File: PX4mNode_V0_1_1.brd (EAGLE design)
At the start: 48.6 x 34.9 mm, 135 parts, among them J201 DF13C-6P-1.25V, J202 DF13C-6P-1.25V, J203 DF13C-6P-1.25V, J301 DF13C-4P-1.25V, J401 DF13C-7P-1.25V, J402 DF13-4P-1.25V, J403 DF13C-4P-1.25V, J404 DF13C-4P-1.25V, J405 DF13C-4P-1.25V, J801 DF13C-3P-1.25V, M3_MOUNT1101 MOUNT-HOLE3.1MM, M3_MOUNT1102 MOUNT-HOLE3.1MM, M3_MOUNT1103 MOUNT-HOLE3.1MM, M3_MOUNT1104 MOUNT-HOLE3.1MM, U101 STM32F4X7VX, U401 MAX3051, U402 MAX3051, X101 3.2x2.5 mm / 24 MHz / 15 ppm

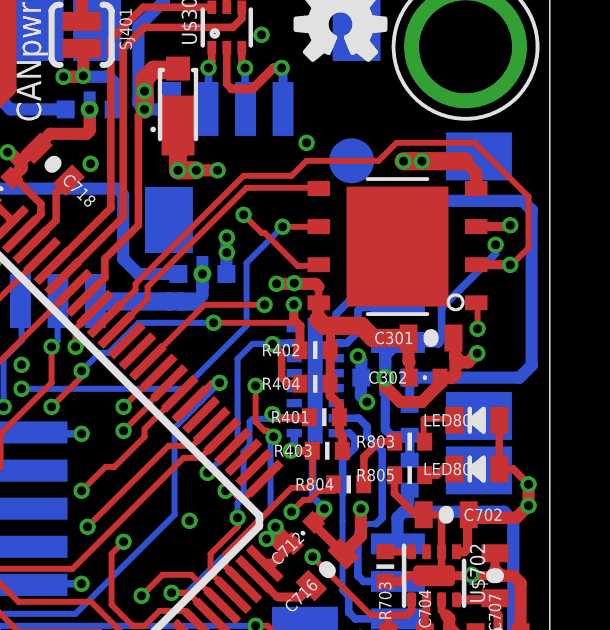
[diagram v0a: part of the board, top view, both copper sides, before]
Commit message: Corrected kyocera filter stop mask on center ground pad
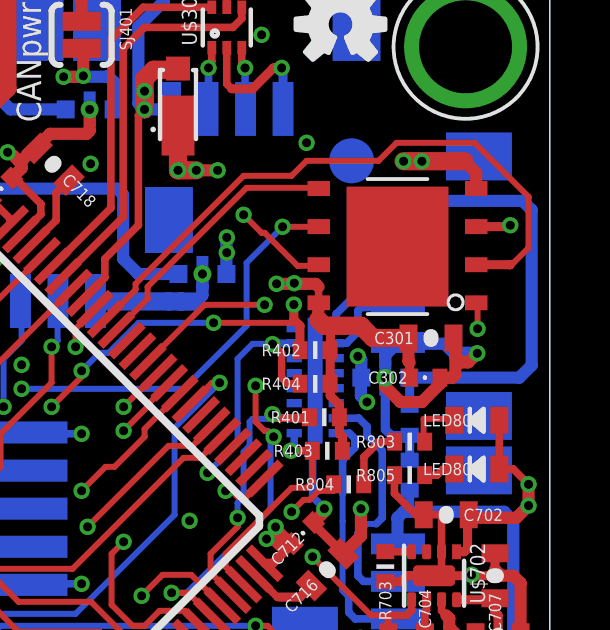
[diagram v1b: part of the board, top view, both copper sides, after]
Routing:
- net GND: track 228.4 -> 225.7 mm, vias 61 -> 60
- net SDIO_D1: vias 1 -> 0
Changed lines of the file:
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@@
 <grid distance="0.1" unitdist="mm" unit="mm" style="dots" multiple="1" display="yes" altdistance="4" altunitdist="mil" altunit="mm"/>
 <layers>
-<layer number="1" name="Top" color="4" fill="1" visible="no" active="yes"/>
-<layer number="2" name="Ground" color="2" fill="10" visible="yes" active="yes"/>
-<layer number="3" name="Horizontal" color="13" fill="15" visible="yes" active="yes"/>
+<layer number="1" name="Top" color="4" fill="1" visible="yes" active="yes"/>
+<layer number="2" name="Ground" color="2" fill="10" visible="no" active="yes"/>
+<layer number="3" name="Horizontal" color="13" fill="15" visible="no" active="yes"/>
 <layer number="4" name="Route4" color="1" fill="4" visible="no" active="no"/>
 <layer number="5" name="Route5" color="4" fill="4" visible="no" active="no"/>
@@
 <layer number="12" name="Route12" color="1" fill="5" visible="no" active="no"/>
 <layer number="13" name="Route13" color="4" fill="5" visible="no" active="no"/>
-<layer number="14" name="Vertical" color="14" fill="15" visible="yes" active="yes"/>
-<layer number="15" name="Power" color="11" fill="15" visible="yes" active="yes"/>
+<layer number="14" name="Vertical" color="14" fill="15" visible="no" active="yes"/>
+<layer number="15" name="Power" color="11" fill="15" visible="no" active="yes"/>
 <layer number="16" name="Bottom" color="1" fill="1" visible="yes" active="yes"/>
 <layer number="17" name="Pads" color="2" fill="1" visible="yes" active="yes"/>
 <layer number="18" name="Vias" color="2" fill="1" visible="yes" active="yes"/>
-<layer number="19" name="Unrouted" color="14" fill="1" visible="yes" active="yes"/>
+<layer number="19" name="Unrouted" color="14" fill="1" visible="no" active="yes"/>
 <layer number="20" name="Dimension" color="15" fill="1" visible="yes" active="yes"/>
 <layer number="21" name="tPlace" color="7" fill="1" visible="yes" active="yes"/>
-<layer number="22" name="bPlace" color="7" fill="1" visible="no" active="yes"/>
+<layer number="22" name="bPlace" color="7" fill="1" visible="yes" active="yes"/>
 <layer number="23" name="tOrigins" color="15" fill="1" visible="yes" active="yes"/>
-<layer number="24" name="bOrigins" color="15" fill="1" visible="no" active="yes"/>
+<layer number="24" name="bOrigins" color="15" fill="1" visible="yes" active="yes"/>
 <layer number="25" name="tNames" color="7" fill="1" visible="no" active="yes"/>
 <layer number="26" name="bNames" color="7" fill="1" visible="no" active="yes"/>
@@
 <layer number="38" name="bTest" color="7" fill="1" visible="no" active="yes"/>
 <layer number="39" name="tKeepout" color="4" fill="11" visible="yes" active="yes"/>
-<layer number="40" name="bKeepout" color="1" fill="11" visible="no" active="yes"/>
+<layer number="40" name="bKeepout" color="1" fill="11" visible="yes" active="yes"/>
 <layer number="41" name="tRestrict" color="4" fill="10" visible="yes" active="yes"/>
-<layer number="42" name="bRestrict" color="1" fill="10" visible="no" active="yes"/>
+<layer number="42" name="bRestrict" color="1" fill="10" visible="yes" active="yes"/>
 <layer number="43" name="vRestrict" color="2" fill="10" visible="no" active="yes"/>
 <layer number="44" name="Drills" color="7" fill="1" visible="no" active="yes"/>
@@
 <layer number="50" name="dxf" color="7" fill="1" visible="no" active="yes"/>
 <layer number="51" name="tDocu" color="7" fill="1" visible="yes" active="yes"/>
-<layer number="52" name="bDocu" color="7" fill="1" visible="no" active="yes"/>
+<layer number="52" name="bDocu" color="7" fill="1" visible="yes" active="yes"/>
 <layer number="53" name="tGND_GNDA" color="7" fill="9" visible="no" active="no"/>
 <layer number="54" name="bGND_GNDA" color="1" fill="9" visible="no" active="no"/>
@@
 <contactref element="U101" pad="66"/>
 <contactref element="U$302" pad="2"/>
-<via x="56.4896" y="27.432" extent="1-16" drill="0.3" diameter="0.55"/>
 <wire x1="55.3554" y1="27.4366" x2="56.485" y2="27.4366" width="0.3048" layer="1"/>
 <wire x1="56.485" y1="27.4366" x2="56.4896" y2="27.432" width="0.3048" layer="1"/>
@@
 <wire x1="28.9" y1="32.2" x2="28.956" y2="32.2072" width="0.254" layer="16"/>
 <wire x1="28.7" y1="32.2" x2="28.556" y2="32.2072" width="0.254" layer="16"/>
-<wire x1="56" y1="27.8" x2="56" y2="28.1" width="0.254" layer="16"/>
-<wire x1="54.2" y1="26" x2="56" y2="27.8" width="0.254" layer="16"/>
-<wire x1="54.2" y1="24.9" x2="54.2" y2="26" width="0.254" layer="16"/>
-<wire x1="54.1" y1="24.8" x2="54.2" y2="24.9" width="0.254" layer="16"/>
-<wire x1="52.9" y1="24.8" x2="54.1" y2="24.8" width="0.254" layer="16"/>
-<wire x1="52.9" y1="24.8" x2="52.7448" y2="24.8458" width="0.254" layer="16"/>
-<wire x1="52.4" y1="23.6" x2="52.4" y2="23.4" width="0.254" layer="16"/>
-<wire x1="52.4" y1="23.4" x2="52.324" y2="23.2728" width="0.254" layer="16"/>
-<wire x1="52.4" y1="23.6" x2="52.324" y2="23.6728" width="0.254" layer="16"/>
 <wire x1="34.3" y1="8.2" x2="34.6" y2="8.2" width="0.254" layer="16"/>
 <wire x1="34.6" y1="8.2" x2="34.6392" y2="8.2296" width="0.254" layer="16"/>
@@
 <wire x1="32.8" y1="9.4" x2="32.8168" y2="9.4" width="0.254" layer="1"/>
 <wire x1="32.8" y1="9.4" x2="32.9852" y2="9.5852" width="0.254" layer="1"/>
-<via x="56" y="28.1" extent="1-16" drill="0.3" diameter="0.55"/>
 <via x="48.3" y="6.5" extent="1-16" drill="0.3" diameter="0.55"/>
 <via x="48" y="14.6" extent="1-16" drill="0.3" diameter="0.55"/>
@@
 <wire x1="47.818" y1="12.9032" x2="45.8216" y2="12.9032" width="0.254" layer="1"/>
 <wire x1="45.8216" y1="12.9032" x2="45.463953125" y2="12.545553125" width="0.254" layer="1"/>
-<wire x1="46.228" y1="27.1272" x2="46.228" y2="27.5272" width="0" layer="19" extent="16-16"/>
+<wire x1="55.4" y1="24.5" x2="54.6" y2="24.5" width="0.4064" layer="16"/>
+<wire x1="54.6" y1="24.5" x2="54.3" y2="24.8" width="0.4064" layer="16"/>
+<wire x1="54.3" y1="24.8" x2="52.7448" y2="24.8" width="0.4064" layer="16"/>
+<wire x1="52.7448" y1="24.8" x2="52.7448" y2="24.8458" width="0.4064" layer="16"/>
+<wire x1="52.324" y1="23.2728" x2="52.324" y2="23.6728" width="0.254" layer="16"/>
+<wire x1="46.228" y1="27.5272" x2="46.228" y2="27.1272" width="0" layer="19" extent="16-16"/>
+<wire x1="55.4" y1="24.5" x2="55.3896" y2="24.5" width="0.254" layer="16"/>
+<wire x1="55.3896" y1="24.5" x2="55.3896" y2="24.484" width="0.254" layer="16"/>
 </signal>
 <signal name="N$4">
@@
 <wire x1="13.46" y1="9.8552" x2="13.46" y2="10.46" width="1.016" layer="15"/>
 <wire x1="13.46" y1="10.46" x2="14.4" y2="11.4" width="1.016" layer="15"/>
-<wire x1="14.4" y1="11.4" x2="16.9" y2="11.4" width="1.016" layer="15"/>
+<wire x1="14.4" y1="11.4" x2="16.9" y2="11.4" width="0.8128" layer="15"/>
 <wire x1="16.9" y1="11.4" x2="17.5" y2="12" width="1.016" layer="15"/>
 <wire x1="17.5" y1="12" x2="17.5" y2="13.8" width="1.016" layer="15"/>

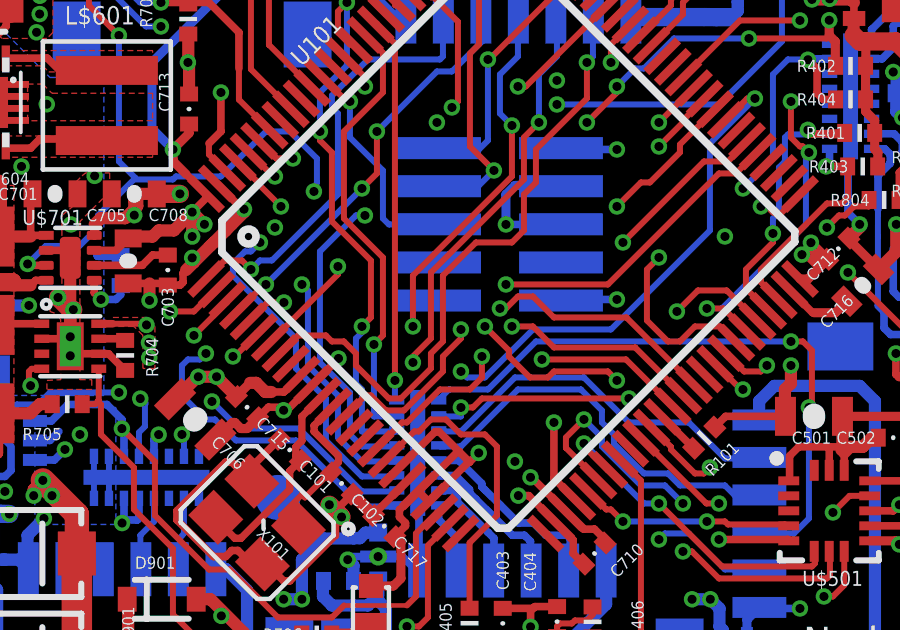
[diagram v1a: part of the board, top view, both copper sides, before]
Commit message: Added nReset SWD connection to !FMU_RESET
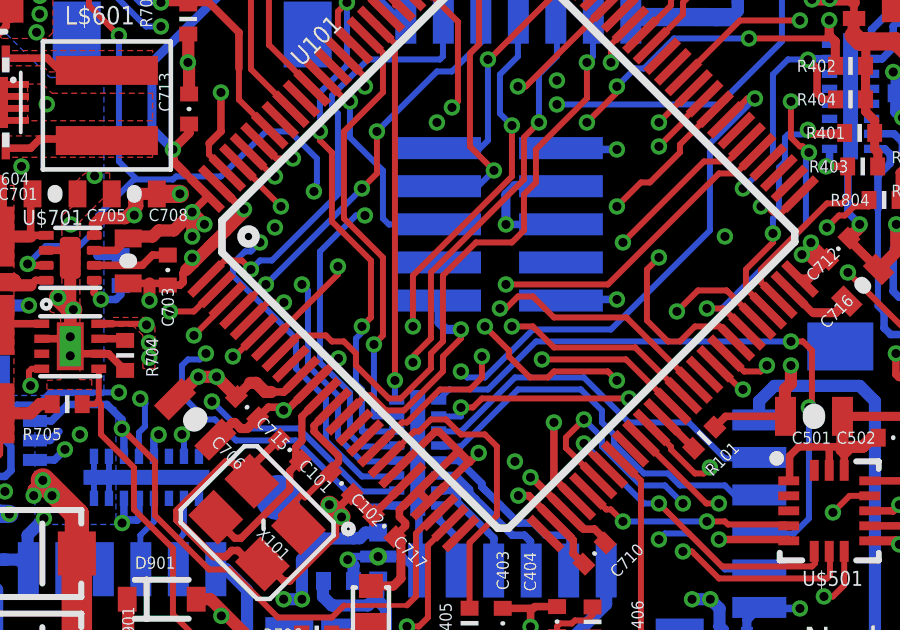
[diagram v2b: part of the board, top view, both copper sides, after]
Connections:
- net FMU-!RESET: now also JX301.10
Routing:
- net FMU-!RESET: track 47.0 -> 48.5 mm
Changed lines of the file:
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@@
 <layer number="17" name="Pads" color="2" fill="1" visible="yes" active="yes"/>
 <layer number="18" name="Vias" color="2" fill="1" visible="yes" active="yes"/>
-<layer number="19" name="Unrouted" color="14" fill="1" visible="no" active="yes"/>
+<layer number="19" name="Unrouted" color="14" fill="1" visible="yes" active="yes"/>
 <layer number="20" name="Dimension" color="15" fill="1" visible="yes" active="yes"/>
 <layer number="21" name="tPlace" color="7" fill="1" visible="yes" active="yes"/>
@@
 <wire x1="23.1568" y1="18.5832" x2="22.5568" y2="17.9832" width="0.2" layer="16"/>
 <wire x1="33.81430625" y1="13.6" x2="33.101496875" y2="12.887190625" width="0.2" layer="1"/>
+<contactref element="JX301" pad="10"/>
+<wire x1="37" y1="15.8" x2="36.5" y2="15.8" width="0.3048" layer="16"/>
+<wire x1="36.5" y1="15.8" x2="36.2712" y2="16.0288" width="0.3048" layer="16"/>
+<wire x1="36.2712" y1="16.0288" x2="36.2712" y2="16.764" width="0.3048" layer="16"/>
 </signal>
 <signal name="N$42" class="1">

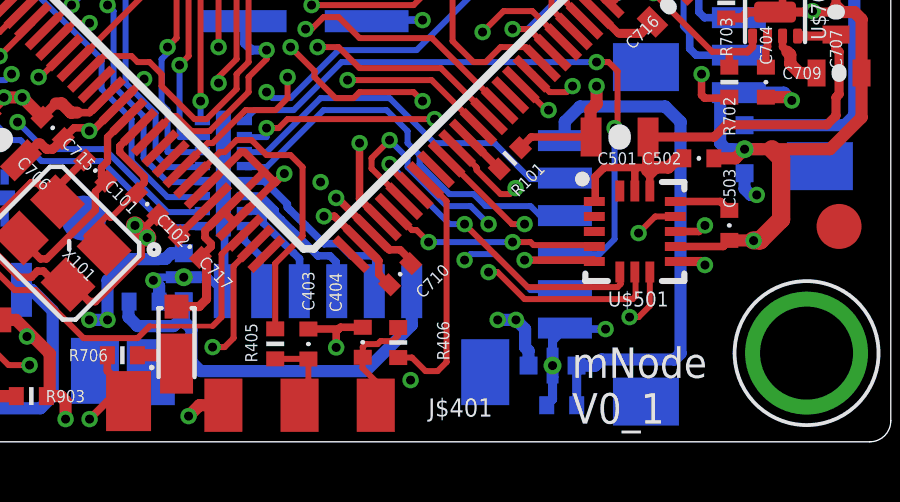
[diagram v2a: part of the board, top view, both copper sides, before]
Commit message: Moved analog connector pads
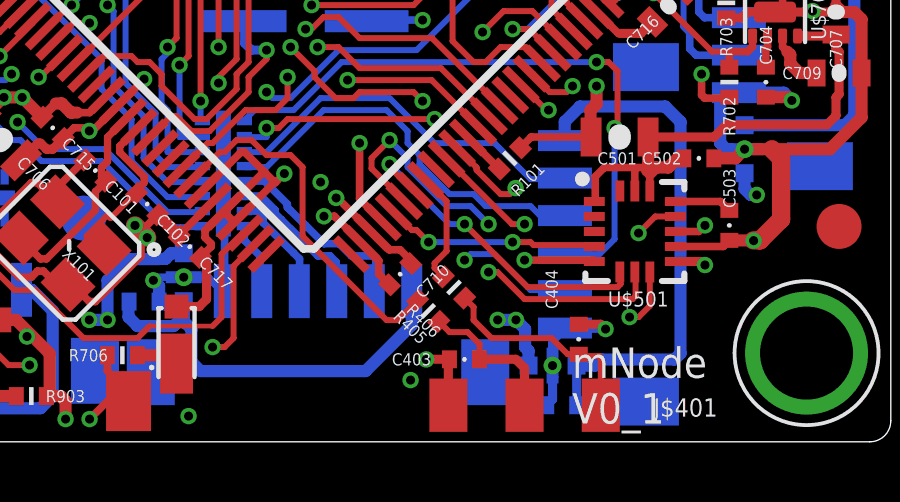
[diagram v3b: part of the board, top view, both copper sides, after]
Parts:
- moved J$401 7.50 mm to (45.6, 3.96)
- moved C404 7.20 mm to (47.4, 6.16)
- moved C403 5.23 mm to (43.6, 5.49), turned to 180 degrees
- moved R405 5.22 mm to (42.4, 7.11), turned to 315 degrees
- moved R406 2.61 mm to (43.2, 7.89), turned to 315 degrees
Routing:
- net FMU_AUX_ADC2: track 8.32 -> 3.84 mm
- net FMU_AUX_ADC2_PROT: track 3.73 -> 7.21 mm
- net FMU_AUX_ADC1_PROT: track 2.77 -> 5.04 mm
- net FMU_AUX_ADC1: track 10.4 -> 12.2 mm
- net GND: track 225.7 -> 225.2 mm

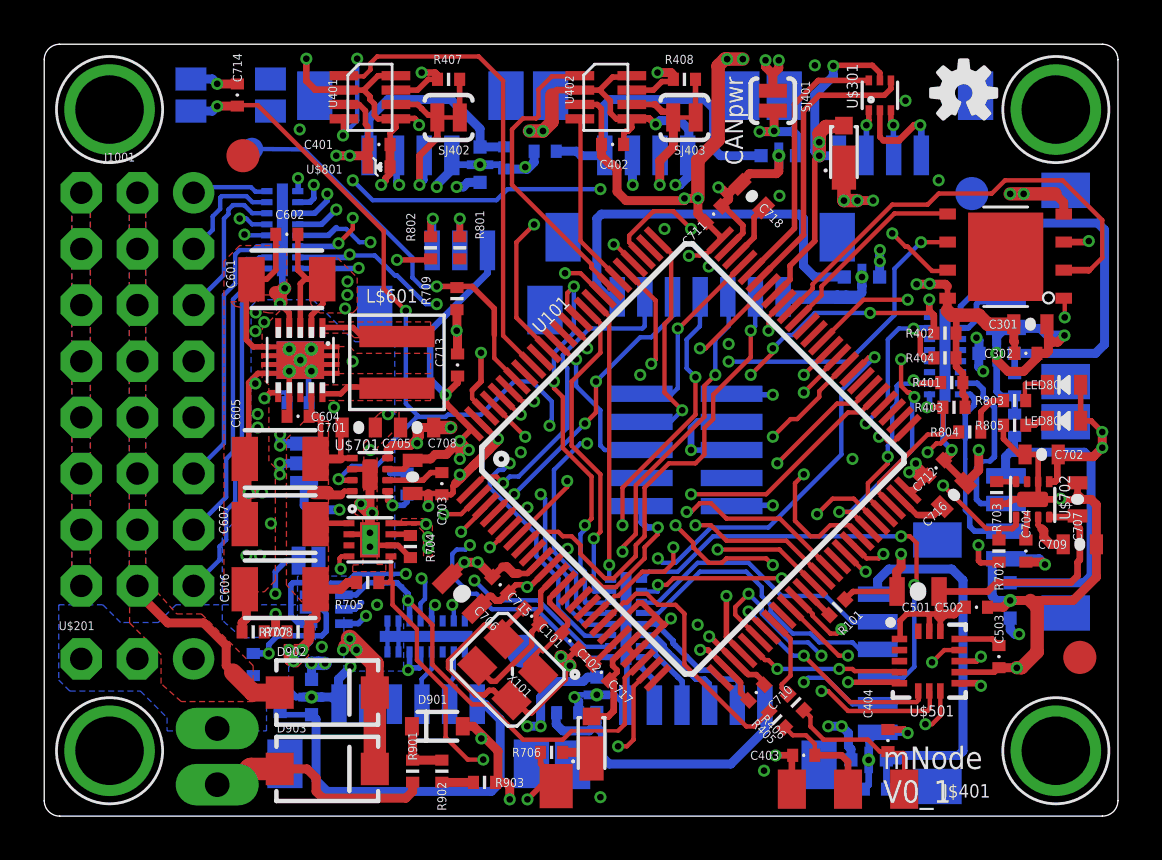
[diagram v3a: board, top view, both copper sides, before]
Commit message: Added extra ground and power connections
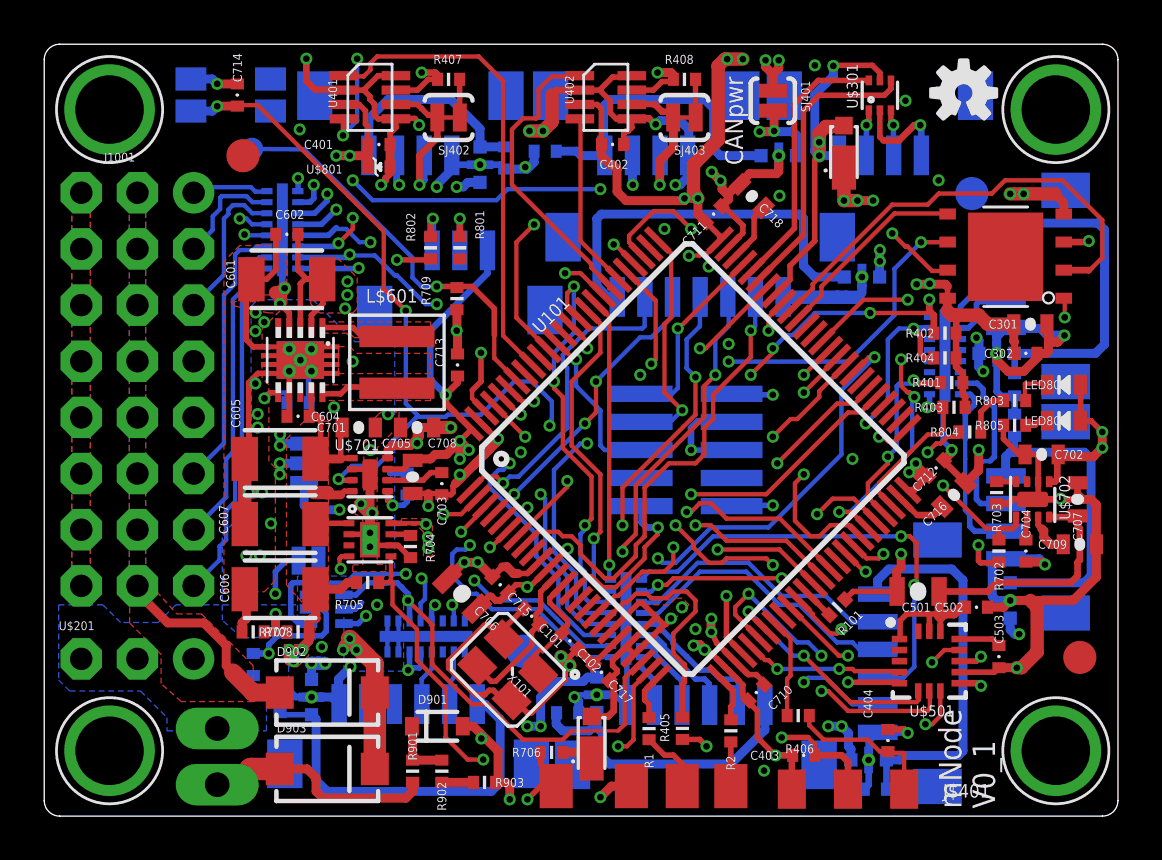
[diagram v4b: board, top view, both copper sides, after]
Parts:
- added JP1, JP2, JP3: M01SMD-4.5X1.5, SparkFun-Connectors:PAD-1.5X4.5
- added R1, R2: 220R, pixhawk2:0402-RES
- moved R405 4.30 mm to (38.1, 6.71), turned to 270 degrees
- moved R406 0.61 mm to (43.3, 7.29), turned to 0 degrees
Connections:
- new net N$19: JP1.P$1, R1.P$1
- new net N$23: JP2.P$1, R2.P$1
- net FMU-CH10: now also R2.P$2
- net FMU-CH9: now also R1.P$2
- net GND: now also JP3.P$1
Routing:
- net GND: track 225.2 -> 231.1 mm, vias 60 -> 62
- net FMU_AUX_ADC1_PROT: track 5.04 -> 9.78 mm, vias 0 -> 2
- net N$19: track 0.00 -> 2.96 mm
- net FMU-CH10: track 0.00 -> 2.18 mm
- net FMU-CH9: track 0.00 -> 2.13 mm
- net N$23: track 0.00 -> 2.00 mm
- net FMU_AUX_ADC1: track 12.2 -> 11.1 mm
- net FMU-VDD_3V3: track 132.1 -> 133.0 mm, vias 23 -> 25
- net FMU_AUX_ADC2: track 3.84 -> 4.57 mm
- added copper zone on layer 1, net FMU-VDD_3V3

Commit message: Simplified GYRO_DRDY route
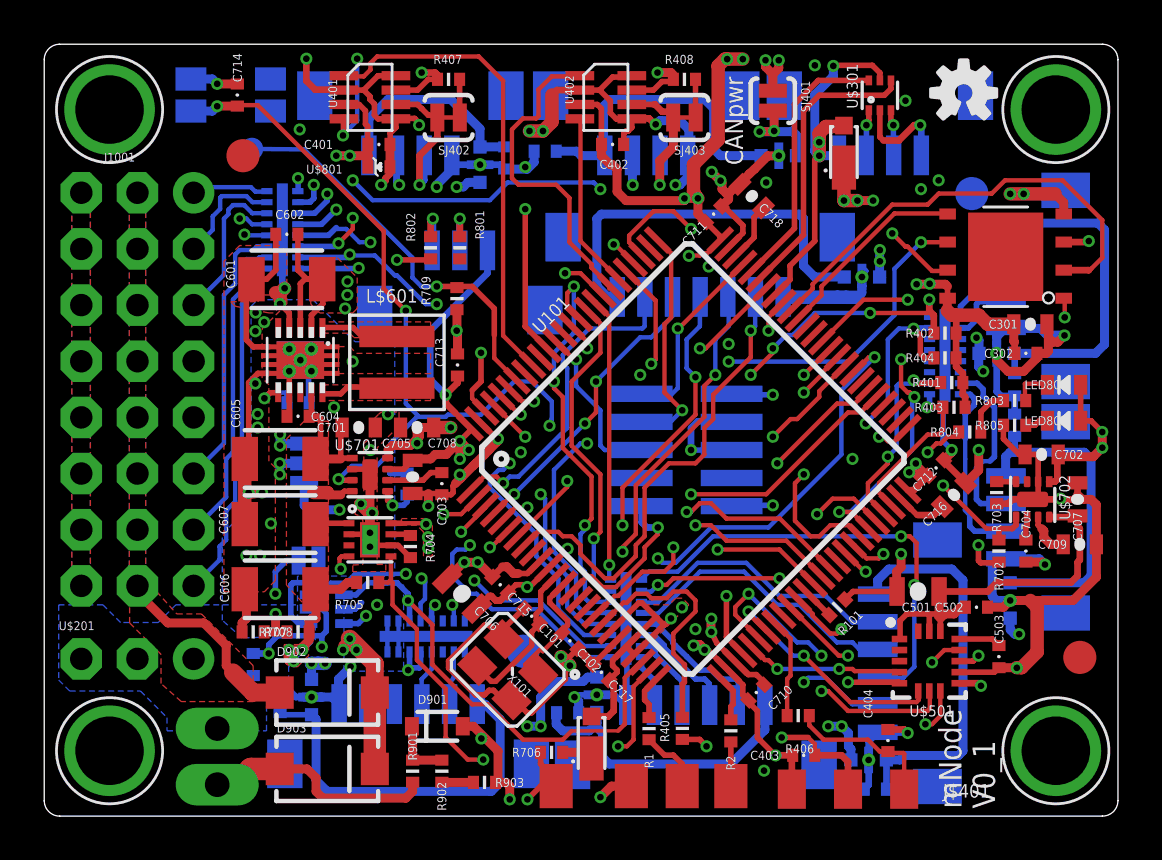
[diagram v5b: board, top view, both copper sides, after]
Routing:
- net ACCEL_DRDY: track 44.0 -> 52.3 mm, vias 5 -> 3
- net CAN1_TX: track 13.9 -> 14.8 mm
- net VDD_IN: track 67.8 -> 68.6 mm
- net FMU-VDD_3V3: track 133.0 -> 133.5 mm
